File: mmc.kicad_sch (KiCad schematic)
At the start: 6 parts, among them IC4 MMC5983MA

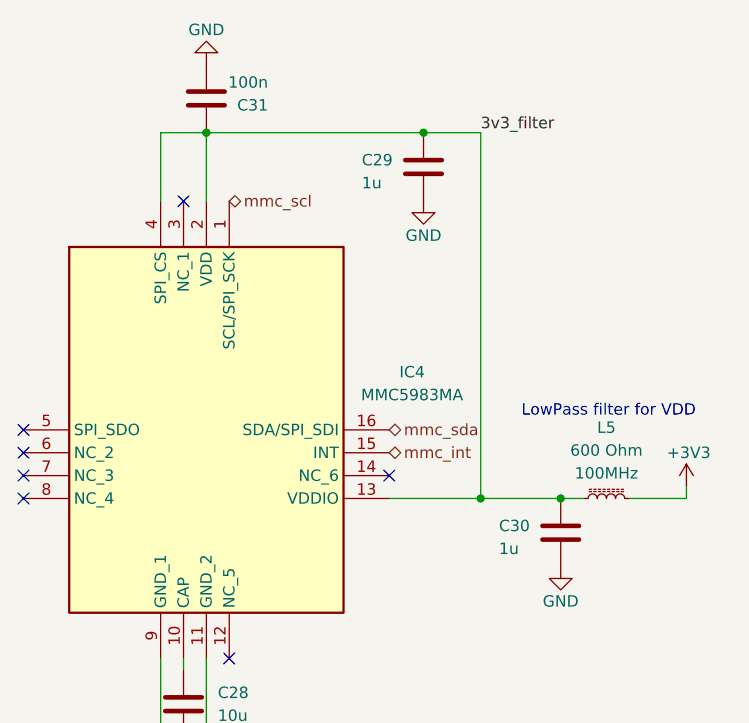
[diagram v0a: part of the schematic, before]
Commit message: feat: rev1 added sdcard
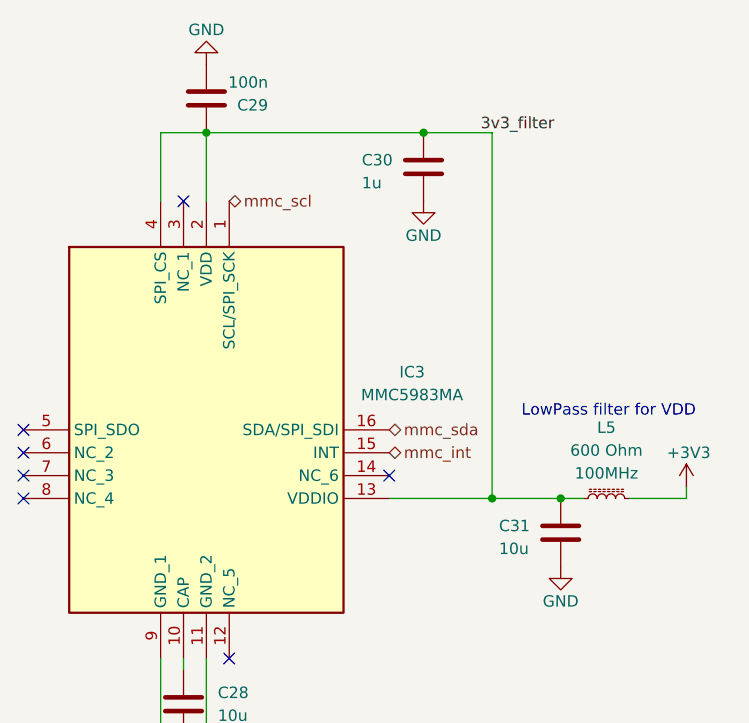
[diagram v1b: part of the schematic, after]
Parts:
- C31: renamed from C30; value 1u -> 10u
- renumbered C31 to C29, C29 to C30, IC4 to IC3
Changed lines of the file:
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@@
 	)
 	(junction
-		(at 97.79 133.35)
+		(at 124.46 63.5)
 		(diameter 0)
 		(color 0 0 0 0)
 	)
 	(junction
-		(at 124.46 63.5)
+		(at 97.79 133.35)
 		(diameter 0)
 		(color 0 0 0 0)
@@
 	)
 	(junction
-		(at 130.81 104.14)
+		(at 132.08 104.14)
 		(diameter 0)
 		(color 0 0 0 0)
@@
 	(wire
 		(pts
-			(xy 120.65 104.14) (xy 130.81 104.14)
+			(xy 120.65 104.14) (xy 132.08 104.14)
 		)
 		(stroke
@@
 	(wire
 		(pts
-			(xy 130.81 63.5) (xy 130.81 104.14)
+			(xy 132.08 63.5) (xy 132.08 104.14)
 		)
 		(stroke
@@
 	(wire
 		(pts
-			(xy 130.81 104.14) (xy 139.7 104.14)
+			(xy 132.08 104.14) (xy 139.7 104.14)
 		)
 		(stroke
@@
 	(wire
 		(pts
-			(xy 124.46 63.5) (xy 130.81 63.5)
+			(xy 124.46 63.5) (xy 132.08 63.5)
 		)
 		(stroke
@@
 		(dnp no)
 		(fields_autoplaced yes)
-		(property "Reference" "IC4"
+		(property "Reference" "IC3"
 			(at 123.19 90.0998 0)
 			(show_name no)
@@
 		(instances
 			(project "engineering_plane"
-				(path "/f9a2ded0-d803-4be9-b2f5-4dda0f6b4d9a/d04d59e8-7cdf-48e0-9592-4dccb7b4f225"
-					(reference "IC4")
+				(path "/f9a2ded0-d803-4be9-b2f5-4dda0f6b4d9a/09acce93-3dbb-42b8-b45b-08d3ba226062"
+					(reference "IC3")
 					(unit 1)
 				)
@@
 		(dnp no)
 		(fields_autoplaced yes)
-		(property "Reference" "#PWR070"
+		(property "Reference" "#PWR074"
 			(at 100.33 49.53 0)
 			(hide yes)
@@
 		(instances
 			(project "engineering_plane"
-				(path "/f9a2ded0-d803-4be9-b2f5-4dda0f6b4d9a/d04d59e8-7cdf-48e0-9592-4dccb7b4f225"
-					(reference "#PWR070")
+				(path "/f9a2ded0-d803-4be9-b2f5-4dda0f6b4d9a/09acce93-3dbb-42b8-b45b-08d3ba226062"
+					(reference "#PWR074")
 					(unit 1)
 				)
@@
 		(dnp no)
 		(fields_autoplaced yes)
-		(property "Reference" "#PWR064"
+		(property "Reference" "#PWR073"
 			(at 97.79 139.7 0)
 			(hide yes)
@@
 		(instances
 			(project "engineering_plane"
-				(path "/f9a2ded0-d803-4be9-b2f5-4dda0f6b4d9a/d04d59e8-7cdf-48e0-9592-4dccb7b4f225"
-					(reference "#PWR064")
+				(path "/f9a2ded0-d803-4be9-b2f5-4dda0f6b4d9a/09acce93-3dbb-42b8-b45b-08d3ba226062"
+					(reference "#PWR073")
 					(unit 1)
 				)
@@
 		(in_pos_files yes)
 		(dnp no)
-		(property "Reference" "C30"
+		(property "Reference" "C31"
 			(at 132.842 107.188 0)
 			(show_name no)
@@
 			)
 		)
-		(property "Value" "1u"
+		(property "Value" "10u"
 			(at 132.842 109.728 0)
 			(show_name no)
@@
 		(instances
 			(project "engineering_plane"
-				(path "/f9a2ded0-d803-4be9-b2f5-4dda0f6b4d9a/d04d59e8-7cdf-48e0-9592-4dccb7b4f225"
-					(reference "C30")
+				(path "/f9a2ded0-d803-4be9-b2f5-4dda0f6b4d9a/09acce93-3dbb-42b8-b45b-08d3ba226062"
+					(reference "C31")
 					(unit 1)
 				)
@@
 		(dnp no)
 		(fields_autoplaced yes)
-		(property "Reference" "#PWR065"
+		(property "Reference" "#PWR075"
 			(at 124.46 77.47 0)
 			(hide yes)
@@
 		(instances
 			(project "engineering_plane"
-				(path "/f9a2ded0-d803-4be9-b2f5-4dda0f6b4d9a/d04d59e8-7cdf-48e0-9592-4dccb7b4f225"
-					(reference "#PWR065")
+				(path "/f9a2ded0-d803-4be9-b2f5-4dda0f6b4d9a/09acce93-3dbb-42b8-b45b-08d3ba226062"
+					(reference "#PWR075")
 					(unit 1)
 				)
@@
 		(instances
 			(project "engineering_plane"
-				(path "/f9a2ded0-d803-4be9-b2f5-4dda0f6b4d9a/d04d59e8-7cdf-48e0-9592-4dccb7b4f225"
+				(path "/f9a2ded0-d803-4be9-b2f5-4dda0f6b4d9a/09acce93-3dbb-42b8-b45b-08d3ba226062"
 					(reference "L5")
 					(unit 1)
@@
 		(instances
 			(project "engineering_plane"
-				(path "/f9a2ded0-d803-4be9-b2f5-4dda0f6b4d9a/d04d59e8-7cdf-48e0-9592-4dccb7b4f225"
+				(path "/f9a2ded0-d803-4be9-b2f5-4dda0f6b4d9a/09acce93-3dbb-42b8-b45b-08d3ba226062"
 					(reference "C28")
 					(unit 1)
@@
 		(in_pos_files yes)
 		(dnp no)
-		(property "Reference" "#PWR067"
+		(property "Reference" "#PWR077"
 			(at 153.67 106.68 0)
 			(hide yes)
@@
 		(instances
 			(project "engineering_plane"
-				(path "/f9a2ded0-d803-4be9-b2f5-4dda0f6b4d9a/d04d59e8-7cdf-48e0-9592-4dccb7b4f225"
-					(reference "#PWR067")
+				(path "/f9a2ded0-d803-4be9-b2f5-4dda0f6b4d9a/09acce93-3dbb-42b8-b45b-08d3ba226062"
+					(reference "#PWR077")
 					(unit 1)
 				)
@@
 		(in_pos_files yes)
 		(dnp no)
-		(property "Reference" "C31"
+		(property "Reference" "C29"
 			(at 107.188 60.452 0)
 			(show_name no)
@@
 		(instances
 			(project "engineering_plane"
-				(path "/f9a2ded0-d803-4be9-b2f5-4dda0f6b4d9a/d04d59e8-7cdf-48e0-9592-4dccb7b4f225"
-					(reference "C31")
+				(path "/f9a2ded0-d803-4be9-b2f5-4dda0f6b4d9a/09acce93-3dbb-42b8-b45b-08d3ba226062"
+					(reference "C29")
 					(unit 1)
 				)
@@
 		(dnp no)
 		(fields_autoplaced yes)
-		(property "Reference" "#PWR066"
+		(property "Reference" "#PWR076"
 			(at 139.7 118.11 0)
 			(hide yes)
@@
 		(instances
 			(project "engineering_plane"
-				(path "/f9a2ded0-d803-4be9-b2f5-4dda0f6b4d9a/d04d59e8-7cdf-48e0-9592-4dccb7b4f225"
-					(reference "#PWR066")
+				(path "/f9a2ded0-d803-4be9-b2f5-4dda0f6b4d9a/09acce93-3dbb-42b8-b45b-08d3ba226062"
+					(reference "#PWR076")
 					(unit 1)
 				)
@@
 		(in_pos_files yes)
 		(dnp no)
-		(property "Reference" "C29"
+		(property "Reference" "C30"
 			(at 117.602 66.548 0)
 			(show_name no)
@@
 		(instances
 			(project "engineering_plane"
-				(path "/f9a2ded0-d803-4be9-b2f5-4dda0f6b4d9a/d04d59e8-7cdf-48e0-9592-4dccb7b4f225"
-					(reference "C29")
+				(path "/f9a2ded0-d803-4be9-b2f5-4dda0f6b4d9a/09acce93-3dbb-42b8-b45b-08d3ba226062"
+					(reference "C30")
 					(unit 1)
 				)

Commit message: feat: final changes, sent to prod
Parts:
- removed C30: 1u, Capacitor_SMD:C_0603_1608Metric, symbol Device:C
- added C16: 1u, Capacitor_SMD:C_0603_1608Metric, symbol Device:C
- L3: renamed from L5; footprint PCM_SparkFun-Capacitor:C_0805_2012Metric -> PCM_SparkFun-Resistor:R_0603_1608Metric
- renumbered C28 to C14, C29 to C15, C31 to C17
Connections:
- net +3V3: now also IC3.13 (VDDIO), IC3.4 (SPI_CS), C16.1
- net 3v3_filter: no longer IC3.13 (VDDIO), IC3.4 (SPI_CS)
- net GND: now also C16.2
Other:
- moved on the sheet: C17, L3

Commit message: Revised componenents, need to route
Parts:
- removed C14, C17: 10u, Capacitor_SMD:C_0603_1608Metric, symbol Device:C
- removed C15: 100n, Capacitor_SMD:C_0603_1608Metric, symbol Device:C
- removed C16: 1u, Capacitor_SMD:C_0603_1608Metric, symbol Device:C
- removed L3: 600 Ohm, PCM_SparkFun-Resistor:R_0603_1608Metric, symbol PCM_SparkFun-Coil:Ferrite_600Ohm_0805_500mA
- added C501, C504: 10uF, PCM_JLCPCB:C_0603, symbol PCM_JLCPCB-Capacitors:0603,10uF,(2)
- added C502: 100nF, PCM_JLCPCB:C_0402, symbol PCM_JLCPCB-Capacitors:0402,100nF,(2)
- added C503: 1uF, PCM_JLCPCB:C_0402, symbol PCM_JLCPCB-Capacitors:0402,1uF
- added FB501: (no value), PCM_JLCPCB:FB_0603, symbol PCM_JLCPCB-Inductors:Ferrite,0603
- added TP501, TP502: 1.0mm, PCM_SparkFun-Connector:TestPoint-1.0mm, symbol PCM_SparkFun-Connector:TestPoint_1.0mm
- renumbered IC3 to IC501
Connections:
- net +3V3: now also C503.1, FB501.2, TP501.1
- net 3v3_filter: now also C502.1, C504.1, FB501.1, TP502.1
- net GND: now also C501.2, C502.2, C503.2, C504.2
- net at IC501.10 (CAP): now also C501.1
- net mmc_scl renamed I2C.SCL
- net mmc_sda renamed I2C.SDA
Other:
- moved on the sheet: IC501

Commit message: finished routing
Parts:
- added TP503: 1.0mm, PCM_SparkFun-Connector:TestPoint-1.0mm, symbol PCM_SparkFun-Connector:TestPoint_1.0mm
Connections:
- net GND: now also TP503.1
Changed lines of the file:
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@@
 	)
 	(junction
+		(at 44.45 111.76)
+		(diameter 0)
+		(color 0 0 0 0)
+	)
+	(junction
 		(at 44.45 46.99)
 		(diameter 0)
@@
 					(unit 1)
 				)
+			)
+		)
+	)
+	(symbol
+		(lib_id "PCM_SparkFun-Connector:TestPoint_1.0mm")
+		(at 44.45 111.76 180)
+		(unit 1)
+		(body_style 1)
+		(exclude_from_sim no)
+		(in_bom yes)
+		(on_board yes)
+		(in_pos_files yes)
+		(dnp no)
+		(fields_autoplaced yes)
+		(property "Reference" "TP503"
+			(at 44.45 116.84 0)
+			(show_name no)
+			(do_not_autoplace yes)
+			(effects
+				(font
+					(size 1.27 1.27)
+				)
+			)
+		)
+		(property "Value" "1.0mm"
+			(at 44.45 107.95 0)
+			(hide yes)
+			(show_name no)
+			(do_not_autoplace no)
+			(effects
+				(font
+					(size 1.27 1.27)
+				)
+			)
+		)
+		(property "Footprint" "PCM_SparkFun-Connector:TestPoint-1.0mm"
+			(at 44.45 105.41 0)
+			(hide yes)
+			(show_name no)
+			(do_not_autoplace no)
+			(effects
+				(font
+					(size 1.27 1.27)
+				)
+			)
+		)
+		(property "Datasheet" ""
+			(at 44.45 104.14 0)
+			(hide yes)
+			(show_name no)
+			(do_not_autoplace no)
+			(effects
+				(font
+					(size 1.27 1.27)
+				)
+			)
+		)
+		(property "Description" "Test Point"
+			(at 44.45 101.6 0)
+			(hide yes)
+			(show_name no)
+			(do_not_autoplace no)
+			(effects
+				(font
+					(size 1.27 1.27)
+				)
+			)
+		)
+		(pin "1"
+		)
+		(instances
+			(project "engineering_plane"
+				(path "/f9a2ded0-d803-4be9-b2f5-4dda0f6b4d9a/09acce93-3dbb-42b8-b45b-08d3ba226062"
+					(reference "TP503")
+					(unit 1)
+				)
